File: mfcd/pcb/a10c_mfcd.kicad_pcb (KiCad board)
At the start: 4 copper layers, 179 x 179 mm, 127 parts, among them J2 Conn_02x13_Odd_Even, Q1 BC817-25LT1G

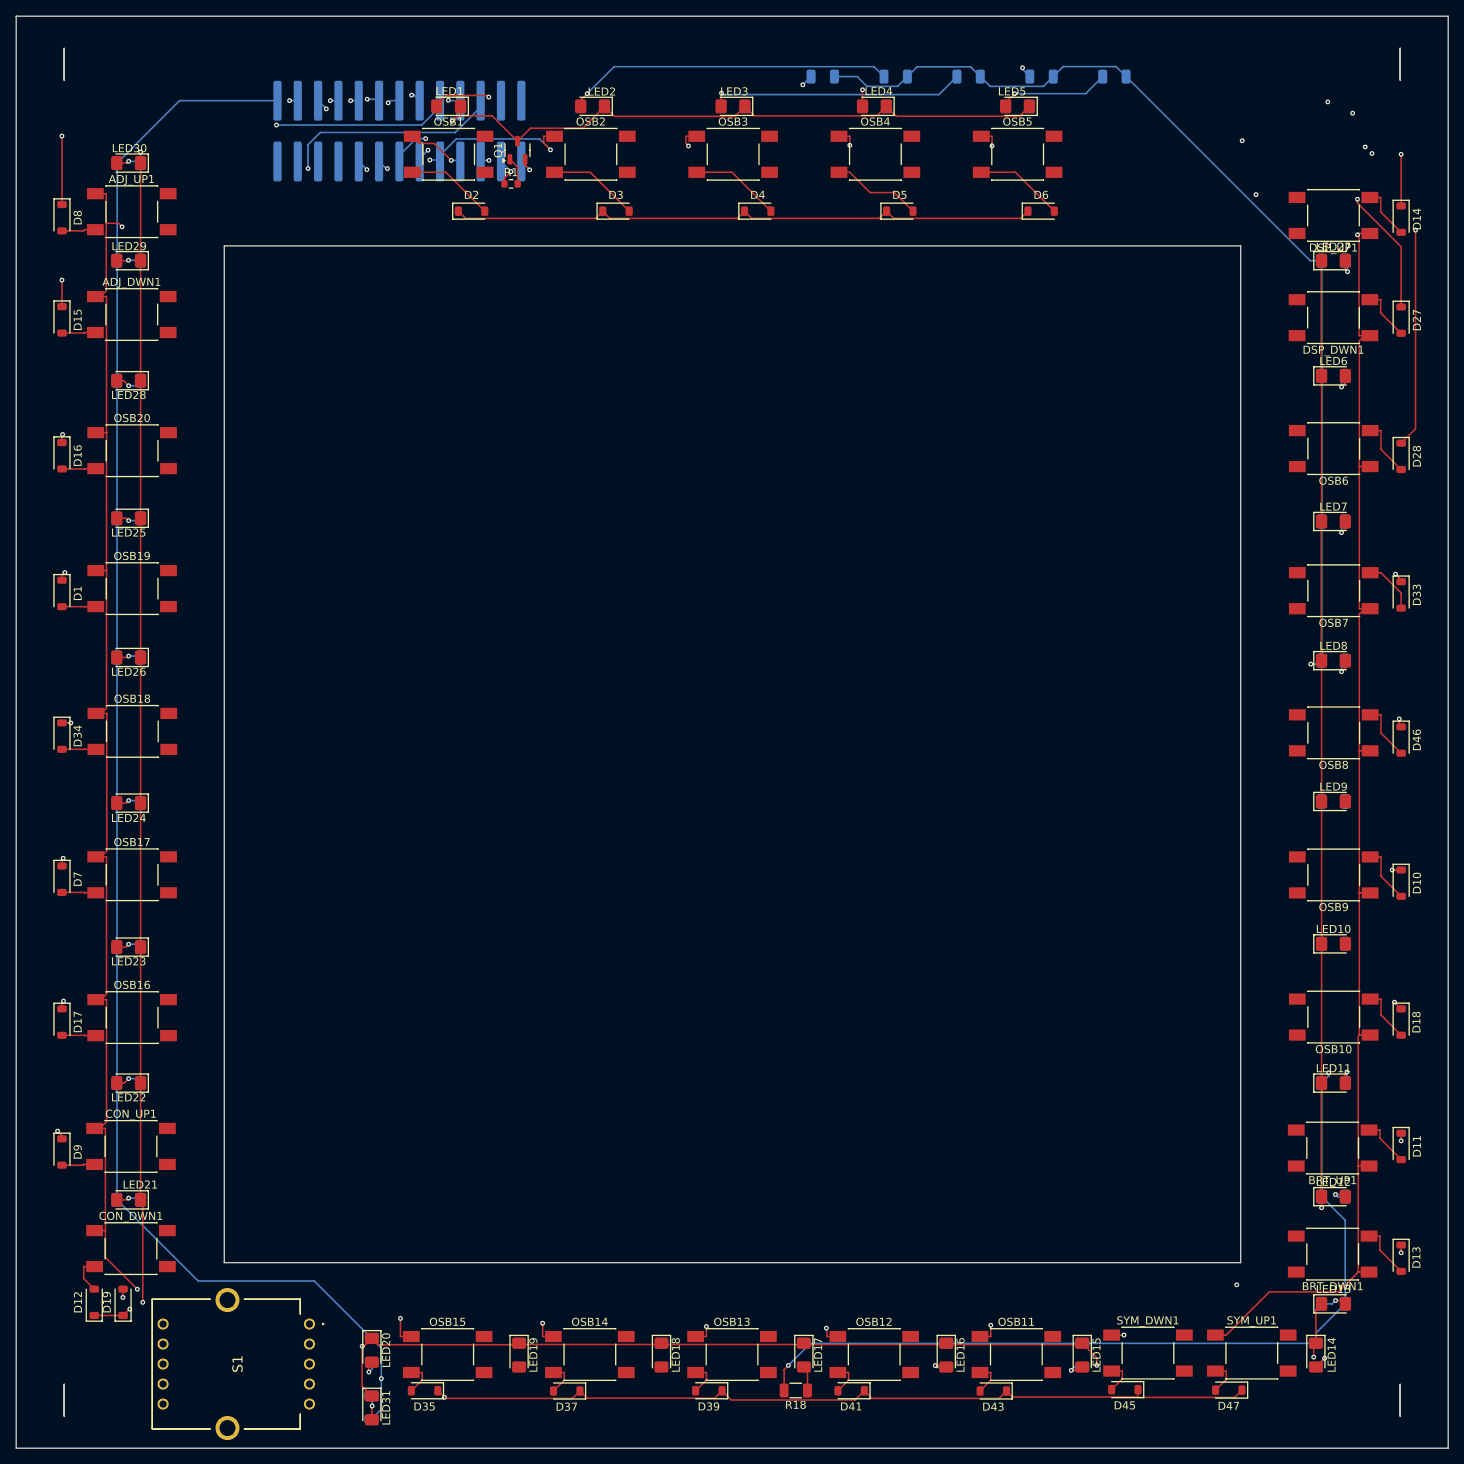
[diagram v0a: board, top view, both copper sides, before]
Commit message: feat(mfcd): updated whole layout to use JST
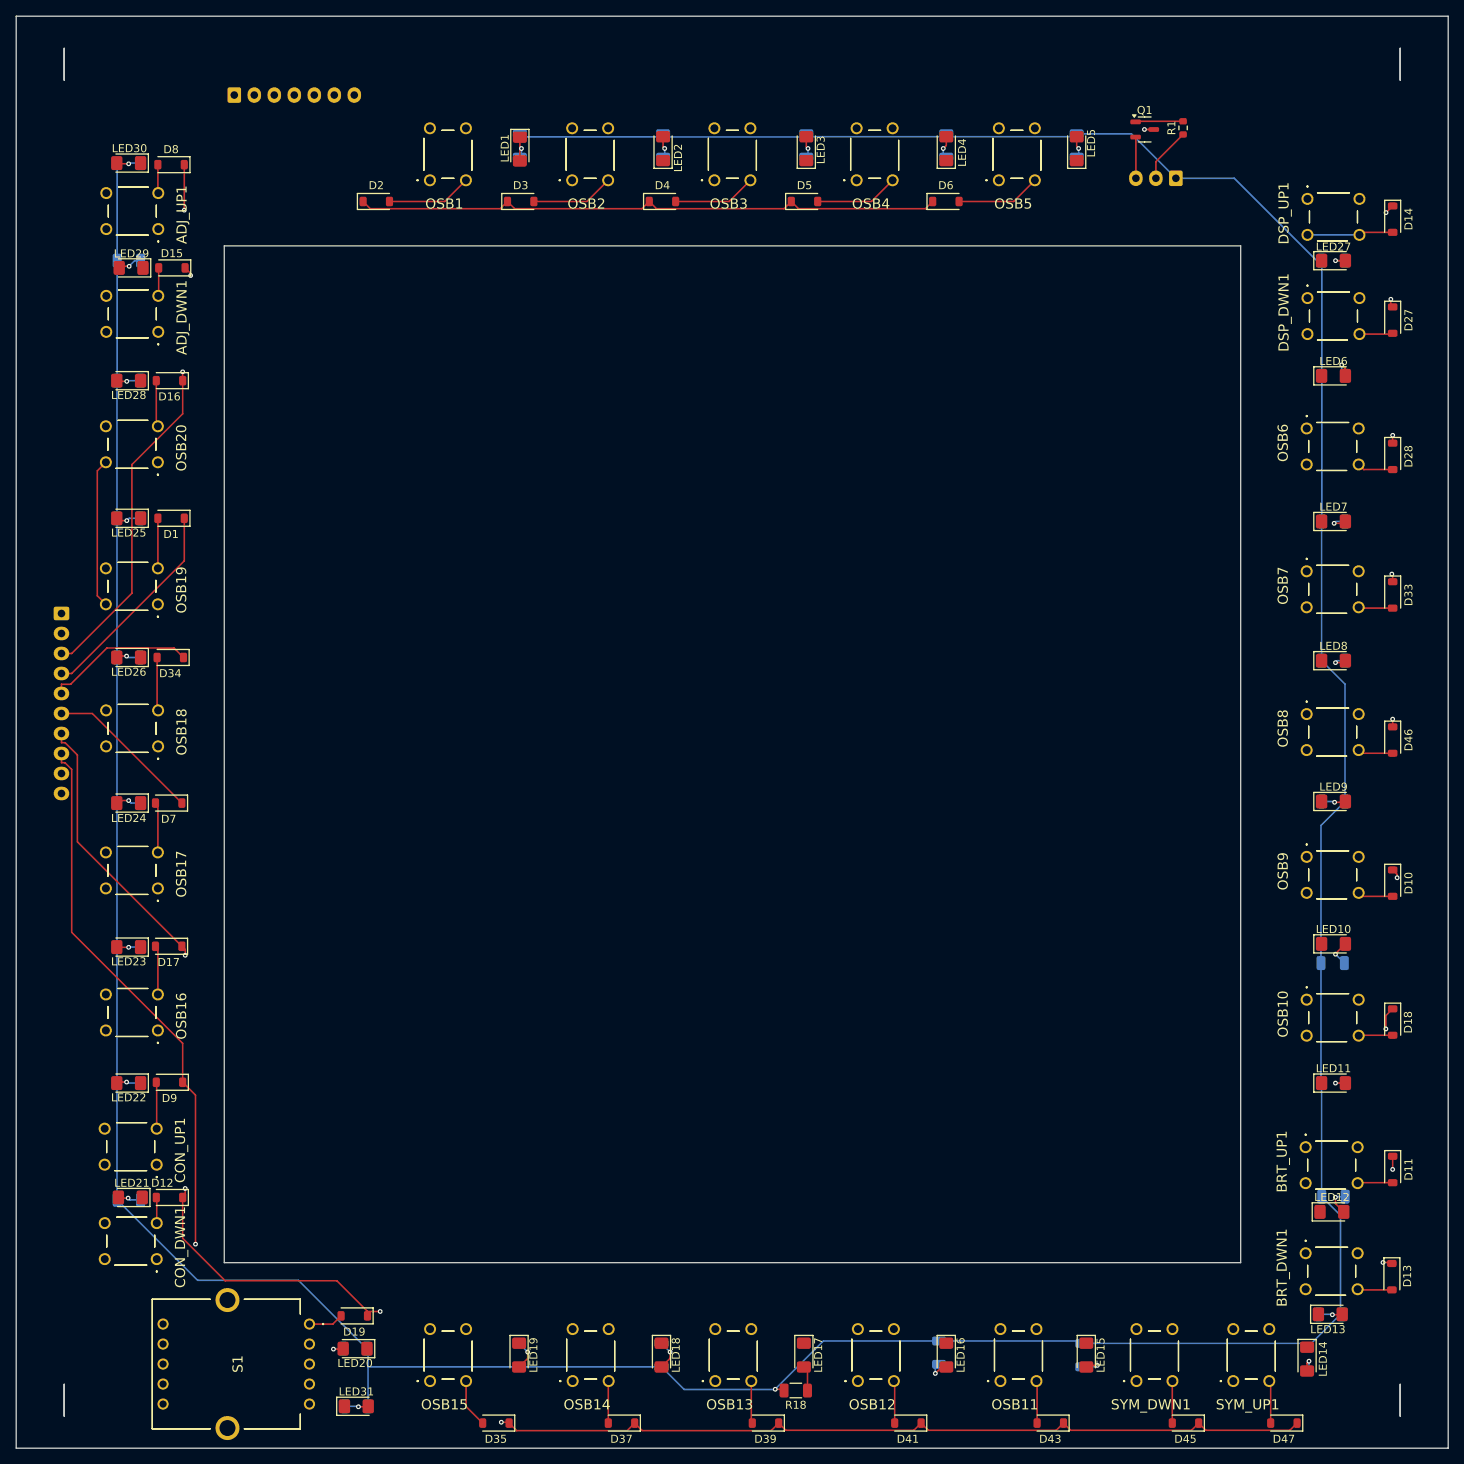
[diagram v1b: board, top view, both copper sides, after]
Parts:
- added J1: Conn_LED, Connector_JST:JST_XH_B3B-XH-A_1x03_P2.50mm_Vertical, B.Cu at (185.7, 80.5)
- added J3: Conn_COLS, Connector_JST:JST_XH_B7B-XH-A_1x07_P2.50mm_Vertical, B.Cu at (68.0, 70.1)
- ADJ_DWN1, ADJ_UP1, BRT_DWN1, BRT_UP1, CON_DWN1, CON_UP1, DSP_DWN1, DSP_UP1, OSB1, OSB10, OSB11, OSB12, OSB13, OSB14, OSB15, OSB16, OSB17, OSB18, OSB19, OSB2, OSB20, OSB3, OSB4, OSB5, OSB6, OSB7, OSB8, OSB9, SYM_DWN1, SYM_UP1: footprint ButtonSwitchSMDEspena:SW_SPST_TL3301_6x6mm_H4.3mm -> Mouser:18259671
- J2: value Conn_02x13_Odd_Even -> Conn_ROWS; footprint Connector_IDC:IDC-Header_2x13_P2.54mm_Vertical_SMD -> Connector_JST:JST_XH_B10B-XH-A_1x10_P2.50mm_Vertical
- LED1, LED10, LED11, LED12, LED13, LED14, LED15, LED16, LED17, LED18, LED19, LED2, LED20, LED21, LED22, LED23, LED24, LED25, LED26, LED27, LED28, LED29, LED3, LED30, LED31, LED4, LED5, LED6, LED7, LED8, LED9: value HSMG-C150 -> 1206
- moved R20 123.1 mm to (103.6, 227.6), turned to -90 degrees
- moved R19 98.5 mm to (121.4, 227.6), turned to -90 degrees
- moved R1 84.3 mm to (186.6, 74.2), turned to 90 degrees
- moved Q1 78.4 mm to (181.8, 74.4), turned to 0 degrees
- moved J2 73.6 mm to (46.4, 134.9), turned to -90 degrees
- moved R2 38.8 mm to (103.7, 76.4), turned to 90 degrees
- moved R3 30.3 mm to (121.6, 76.4), turned to 90 degrees
- moved D19 28.9 mm to (83.0, 222.7), turned to 180 degrees
- moved R4 22.0 mm to (139.5, 76.4), turned to 90 degrees
- moved D34 16.7 mm to (60.0, 140.4), turned to 180 degrees
- moved D1 16.6 mm to (60.1, 123.0), turned to 180 degrees
- moved D16 16.4 mm to (59.9, 105.8), turned to 180 degrees
- moved D7 16.4 mm to (59.8, 158.6), turned to 180 degrees
- moved D17 16.4 mm to (59.8, 176.5), turned to 180 degrees
- moved D12 16.1 mm to (59.9, 207.9), turned to 180 degrees
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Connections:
- J2 pad 1: GND -> ROW0
- J2 pad 10: ROW7 -> ROW9
- J2 pad 2: unconnected-(J2-Pin_2-Pad2) -> ROW1
- J2 pad 3: LED -> ROW2
- J2 pad 4: unconnected-(J2-Pin_4-Pad4) -> ROW3
- J2 pad 5: COL0 -> ROW4
- J2 pad 6: ROW9 -> ROW5
- J2 pad 7: COL1 -> ROW6
- J2 pad 8: ROW8 -> ROW7
- J2 pad 9: COL2 -> ROW8
- LED1 pad 1: Net-(LED1-K) -> Net-(LED1-A)
- LED10 pad 1: Net-(LED1-K) -> unconnected-(LED10-K-Pad1)
- LED11 pad 1: Net-(LED1-K) -> unconnected-(LED11-K-Pad1)
- LED12 pad 1: Net-(LED1-K) -> unconnected-(LED12-K-Pad1)
- LED13 pad 1: Net-(LED1-K) -> unconnected-(LED13-K-Pad1)
- LED14 pad 1: Net-(LED1-K) -> unconnected-(LED14-K-Pad1)
- LED15 pad 1: Net-(LED1-K) -> unconnected-(LED15-K-Pad1)
- LED16 pad 1: Net-(LED1-K) -> unconnected-(LED16-K-Pad1)
- LED17 pad 1: Net-(LED1-K) -> unconnected-(LED17-K-Pad1)
- LED18 pad 1: Net-(LED1-K) -> unconnected-(LED18-K-Pad1)
- LED19 pad 1: Net-(LED1-K) -> unconnected-(LED19-K-Pad1)
- LED2 pad 1: Net-(LED1-K) -> unconnected-(LED2-K-Pad1)
- LED20 pad 1: Net-(LED1-K) -> unconnected-(LED20-K-Pad1)
- LED21 pad 1: Net-(LED1-K) -> unconnected-(LED21-K-Pad1)
- LED22 pad 1: Net-(LED1-K) -> unconnected-(LED22-K-Pad1)
- LED23 pad 1: Net-(LED1-K) -> unconnected-(LED23-K-Pad1)
- LED24 pad 1: Net-(LED1-K) -> unconnected-(LED24-K-Pad1)
- LED25 pad 1: Net-(LED1-K) -> unconnected-(LED25-K-Pad1)
- LED26 pad 1: Net-(LED1-K) -> unconnected-(LED26-K-Pad1)
- LED27 pad 1: Net-(LED1-K) -> unconnected-(LED27-K-Pad1)
- LED28 pad 1: Net-(LED1-K) -> unconnected-(LED28-K-Pad1)
- LED29 pad 1: Net-(LED1-K) -> unconnected-(LED29-K-Pad1)
- LED3 pad 1: Net-(LED1-K) -> unconnected-(LED3-K-Pad1)
- LED30 pad 1: Net-(LED1-K) -> unconnected-(LED30-K-Pad1)
- LED31 pad 1: Net-(LED1-K) -> unconnected-(LED31-K-Pad1)
- LED4 pad 1: Net-(LED1-K) -> unconnected-(LED4-K-Pad1)
- LED5 pad 1: Net-(LED1-K) -> unconnected-(LED5-K-Pad1)
- LED6 pad 1: Net-(LED1-K) -> unconnected-(LED6-K-Pad1)
- LED7 pad 1: Net-(LED1-K) -> unconnected-(LED7-K-Pad1)
- LED8 pad 1: Net-(LED1-K) -> unconnected-(LED8-K-Pad1)
- LED9 pad 1: Net-(LED1-K) -> unconnected-(LED9-K-Pad1)
- Q1 pad 3: Net-(LED1-K) -> Net-(LED1-A)
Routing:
- net Net-(LED1-K): track 570.3 -> 0.00 mm, vias 7 -> 0
- net ROW8: track 348.3 -> 223.0 mm
- net ROW6: track 371.3 -> 248.5 mm, vias 4 -> 2
- net ROW7: track 343.5 -> 228.6 mm, vias 3 -> 2
- net ROW9: track 312.7 -> 218.6 mm, vias 2 -> 1
- net ROW5: track 337.5 -> 287.5 mm, vias 4 -> 1
- net COL6: track 292.5 -> 341.5 mm, vias 2 -> 0
- net Net-(LED2-A): track 40.9 -> 2.72 mm
- net Net-(LED1-A): track 48.7 -> 84.3 mm
- net Net-(LED3-A): track 32.1 -> 2.73 mm
- net ROW0: track 188.9 -> 214.0 mm, vias 3 -> 2
- net Net-(LED4-A): track 24.7 -> 2.86 mm, vias 2 -> 1
- net Net-(D19-A): track 25.8 -> 4.37 mm, vias 1 -> 0
- net COL3: track 290.0 -> 308.8 mm, vias 3 -> 0
- net COL2: track 254.2 -> 272.9 mm, vias 3 -> 0
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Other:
- board text added: "5V"
- board text added: "A10C_II_MFCD_GAMEINTERFACE_v1.0"
- board text added: "COL0"
- board text added: "COL1"
- board text added: "COL2"
- board text added: "COL3"
- board text added: "COL4"
- board text added: "COL5"
- board text added: "COL6"
- board text added: "GND"
- board text added: "LED"
- board text added: "ROW0"
- board text added: "ROW9"
- board text removed: "--- --- --- --- COL6 COL5 COL4 COL3 COL2 COL1 COL0 LED GND"
- board text removed: "5V ROW0 ROW1 ROW2 ROW3 ROW4 ROW5 ROW6 ROW7 ROW8 ROW9 --- ---"
- board text removed: "A10C-II MFCD JOYSTICK by w3z315 (and Rust as motivation guy)"

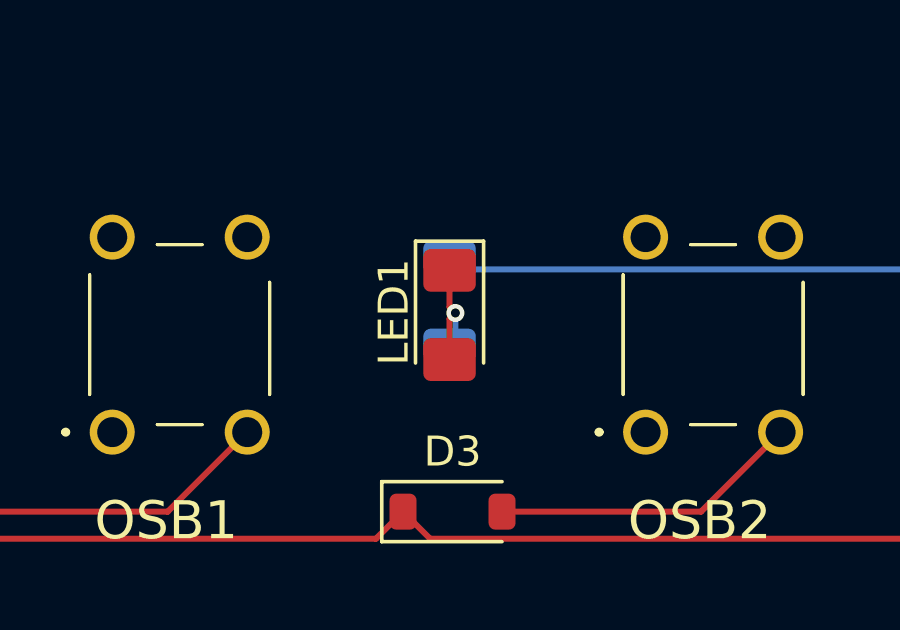
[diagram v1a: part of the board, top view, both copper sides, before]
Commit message: feat(mfcd): added initial arduino code
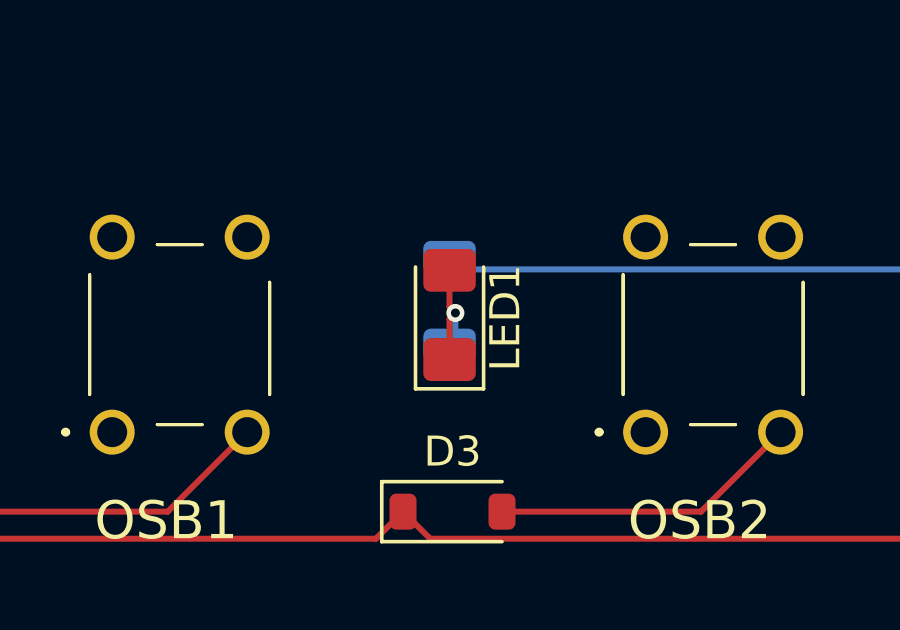
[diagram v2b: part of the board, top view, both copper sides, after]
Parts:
- turned LED1 to 90 degrees
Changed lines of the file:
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@@
 	(footprint "LED_SMD:LED_1206_3216Metric_Pad1.42x1.75mm_HandSolder"
 		(layer "F.Cu")
-		(at 103.7 76.845 -90)
+		(at 103.7 76.845 90)
 		(descr "LED SMD 1206 (3216 Metric), square (rectangular) end terminal, IPC_7351 nominal, (Body size source: http://www.tortai-tech.com/upload/download/2011102023233369053.pdf), generated with kicad-footprint-generator")
 		(tags "LED handsolder")
 		(property "Reference" "LED1"
-			(at -0.0975 1.86 90)
+			(at -0.0975 1.86 270)
 			(layer "F.SilkS")
 			(effects
@@
 		)
 		(property "Value" "1206"
-			(at 0 1.82 90)
+			(at 0 1.82 270)
 			(layer "F.Fab")
 			(effects
@@
 		)
 		(property "Footprint" "LED_SMD:LED_1206_3216Metric_Pad1.42x1.75mm_HandSolder"
-			(at 0 0 -90)
+			(at 0 0 90)
 			(unlocked yes)
 			(layer "F.Fab")
@@
 		)
 		(property "Datasheet" ""
-			(at 0 0 -90)
+			(at 0 0 90)
 			(unlocked yes)
 			(layer "F.Fab")
@@
 		)
 		(property "Description" "Light emitting diode"
-			(at 0 0 -90)
+			(at 0 0 90)
 			(unlocked yes)
 			(layer "F.Fab")
@@
 		)
 		(property "Height" "1.2"
-			(at 0 0 -90)
+			(at 0 0 90)
 			(unlocked yes)
 			(layer "F.Fab")
@@
 		)
 		(property "Mouser Part Number" "630-HSMG-C150"
-			(at 0 0 -90)
+			(at 0 0 90)
 			(unlocked yes)
 			(layer "F.Fab")
@@
 		)
 		(property "Mouser Price/Stock" "https://www.mouser.co.uk/ProductDetail/Broadcom-Avago/HSMG-C150?qs=YDL0qNrpDT6zJe9nNPPiZQ%3D%3D"
-			(at 0 0 -90)
+			(at 0 0 90)
 			(unlocked yes)
 			(layer "F.Fab")
@@
 		)
 		(property "Manufacturer_Name" "Avago Technologies"
-			(at 0 0 -90)
+			(at 0 0 90)
 			(unlocked yes)
 			(layer "F.Fab")
@@
 		)
 		(property "Manufacturer_Part_Number" "HSMG-C150"
-			(at 0 0 -90)
+			(at 0 0 90)
 			(unlocked yes)
 			(layer "F.Fab")
@@
 		(attr smd)
 		(fp_line
+			(start 1.6 -1.135)
+			(end -2.46 -1.135)
+			(stroke
+				(width 0.12)
+				(type solid)
+			)
+			(layer "F.SilkS")
+		)
+		(fp_line
+			(start -2.46 -1.135)
+			(end -2.46 1.135)
+			(stroke
+				(width 0.12)
+				(type solid)
+			)
+			(layer "F.SilkS")
+		)
+		(fp_line
 			(start -2.46 1.135)
 			(end 1.6 1.135)
@@
 		)
 		(fp_line
-			(start -2.46 -1.135)
-			(end -2.46 1.135)
-			(stroke
-				(width 0.12)
-				(type solid)
-			)
-			(layer "F.SilkS")
-		)
-		(fp_line
-			(start 1.6 -1.135)
-			(end -2.46 -1.135)
-			(stroke
-				(width 0.12)
-				(type solid)
-			)
-			(layer "F.SilkS")
+			(start 2.45 -1.12)
+			(end 2.45 1.12)
+			(stroke
+				(width 0.05)
+				(type solid)
+			)
+			(layer "F.CrtYd")
+		)
+		(fp_line
+			(start -2.45 -1.12)
+			(end 2.45 -1.12)
+			(stroke
+				(width 0.05)
+				(type solid)
+			)
+			(layer "F.CrtYd")
+		)
+		(fp_line
+			(start 2.45 1.12)
+			(end -2.45 1.12)
+			(stroke
+				(width 0.05)
+				(type solid)
+			)
+			(layer "F.CrtYd")
 		)
 		(fp_line
@@
 		)
 		(fp_line
-			(start 2.45 1.12)
-			(end -2.45 1.12)
-			(stroke
-				(width 0.05)
-				(type solid)
-			)
-			(layer "F.CrtYd")
-		)
-		(fp_line
-			(start -2.45 -1.12)
-			(end 2.45 -1.12)
-			(stroke
-				(width 0.05)
-				(type solid)
-			)
-			(layer "F.CrtYd")
-		)
-		(fp_line
-			(start 2.45 -1.12)
-			(end 2.45 1.12)
-			(stroke
-				(width 0.05)
-				(type solid)
-			)
-			(layer "F.CrtYd")
+			(start 1.6 -0.8)
+			(end -1.2 -0.8)
+			(stroke
+				(width 0.1)
+				(type solid)
+			)
+			(layer "F.Fab")
+		)
+		(fp_line
+			(start -1.2 -0.8)
+			(end -1.6 -0.4)
+			(stroke
+				(width 0.1)
+				(type solid)
+			)
+			(layer "F.Fab")
+		)
+		(fp_line
+			(start -1.6 -0.4)
+			(end -1.6 0.8)
+			(stroke
+				(width 0.1)
+				(type solid)
+			)
+			(layer "F.Fab")
+		)
+		(fp_line
+			(start 1.6 0.8)
+			(end 1.6 -0.8)
+			(stroke
+				(width 0.1)
+				(type solid)
+			)
+			(layer "F.Fab")
 		)
 		(fp_line
@@
 			(layer "F.Fab")
 		)
-		(fp_line
-			(start 1.6 0.8)
-			(end 1.6 -0.8)
-			(stroke
-				(width 0.1)
-				(type solid)
-			)
-			(layer "F.Fab")
-		)
-		(fp_line
-			(start -1.6 -0.4)
-			(end -1.6 0.8)
-			(stroke
-				(width 0.1)
-				(type solid)
-			)
-			(layer "F.Fab")
-		)
-		(fp_line
-			(start -1.2 -0.8)
-			(end -1.6 -0.4)
-			(stroke
-				(width 0.1)
-				(type solid)
-			)
-			(layer "F.Fab")
-		)
-		(fp_line
-			(start 1.6 -0.8)
-			(end -1.2 -0.8)
-			(stroke
-				(width 0.1)
-				(type solid)
-			)
-			(layer "F.Fab")
-		)
 		(fp_text user "${REFERENCE}"
-			(at 0 0 90)
+			(at 0 0 270)
 			(layer "F.Fab")
 			(effects
@@
 		)
 		(pad "1" smd roundrect
-			(at -1.4875 0 270)
+			(at -1.4875 0 90)
 			(size 1.425 1.75)
 			(layers "F.Cu" "F.Paste" "F.Mask")
@@
 		)
 		(pad "2" smd roundrect
-			(at 1.4875 0 270)
+			(at 1.4875 0 90)
 			(size 1.425 1.75)
 			(layers "F.Cu" "F.Paste" "F.Mask")
